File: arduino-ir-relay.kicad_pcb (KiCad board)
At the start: 2 copper layers, 55.9 x 69.9 mm, 17 parts, among them J0 Screw_Terminal_01x02, J1 Conn_02x03_Row_Letter_First, J2 Conn_02x03_Row_Letter_First, J3 Conn_02x03_Row_Letter_First, J4 Conn_02x03_Row_Letter_First

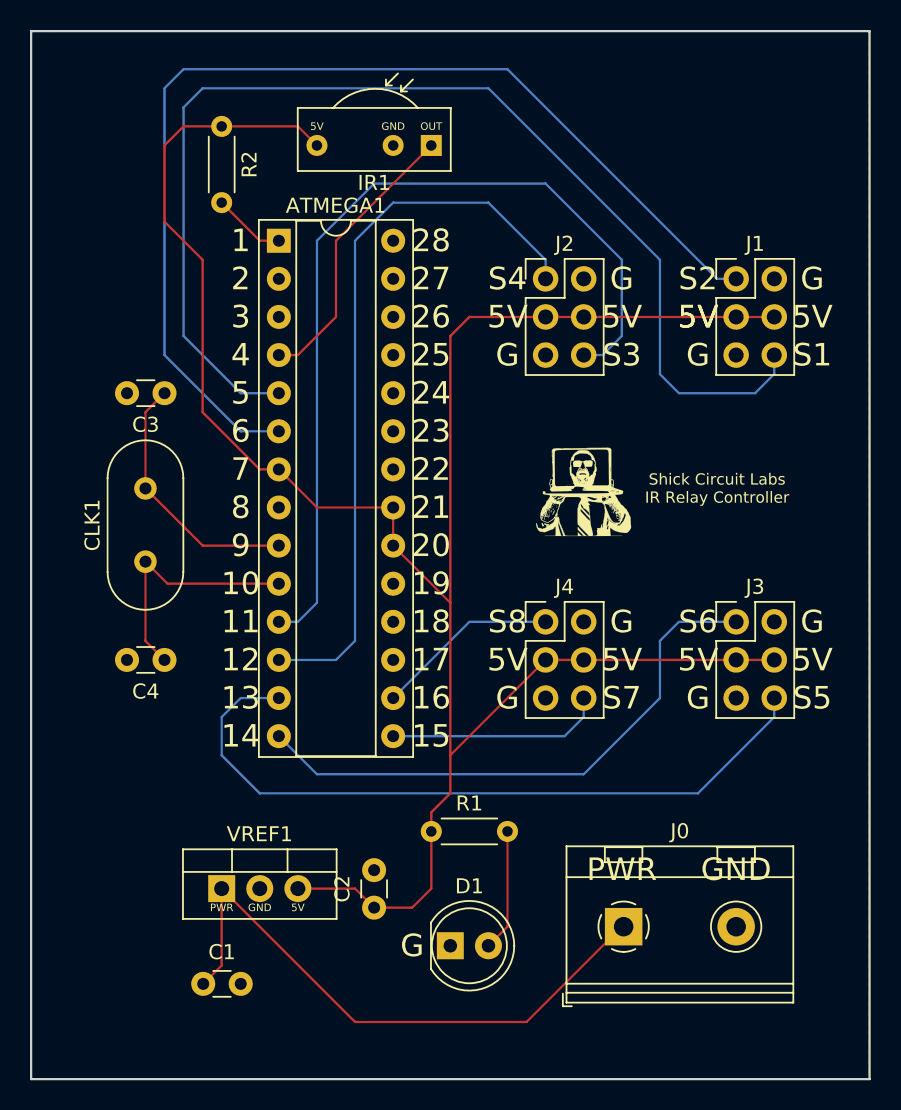
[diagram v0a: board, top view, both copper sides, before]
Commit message: Updated for Kicad 5
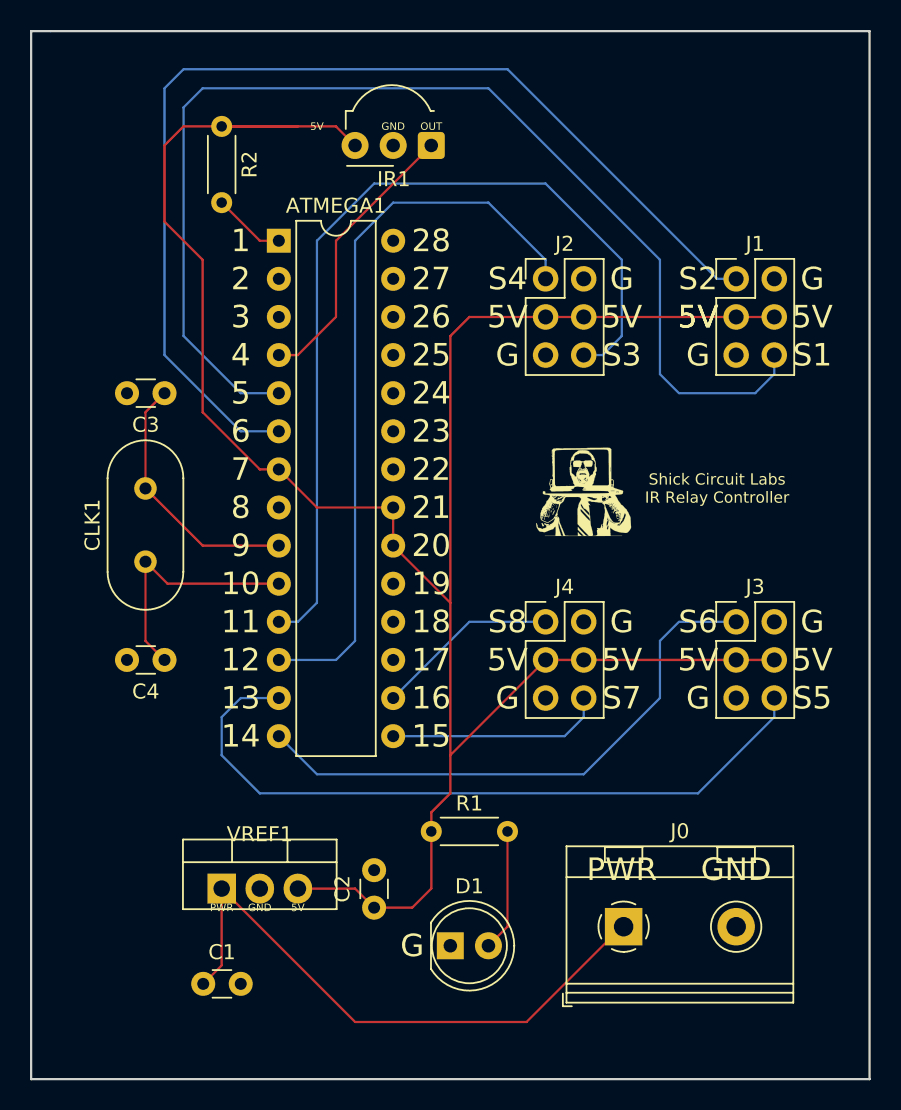
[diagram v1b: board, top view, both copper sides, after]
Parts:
- ATMEGA1: value ATMEGA328P-PU -> ATmega328P-PU; footprint Housings_DIP:DIP-28_W7.62mm_Socket -> Package_DIP:DIP-28_W7.62mm
- C1, C2, C3, C4: footprint Capacitors_THT:C_Disc_D3.0mm_W1.6mm_P2.50mm -> Capacitor_THT:C_Disc_D3.0mm_W1.6mm_P2.50mm
- CLK1: footprint Crystals:Crystal_HC49-U_Vertical -> Crystal:Crystal_HC49-U_Vertical
- D1: footprint LEDs:LED_D5.0mm -> LED_THT:LED_D5.0mm
- IR1: footprint Opto-Devices:IRReceiver_Vishay_CAST-3pin -> OptoDevice:Vishay_MOLD-3Pin
- R1, R2: footprint Resistors_THT:R_Axial_DIN0204_L3.6mm_D1.6mm_P5.08mm_Horizontal -> Resistor_THT:R_Axial_DIN0204_L3.6mm_D1.6mm_P5.08mm_Horizontal
- VREF1: footprint TO_SOT_Packages_THT:TO-220-3_Vertical -> Package_TO_SOT_THT:TO-220-3_Vertical
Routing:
- net 5V: track 146.9 -> 154.6 mm
